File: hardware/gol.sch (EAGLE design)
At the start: 70 parts, among them J1 TC2050-IDC, J2 2057-MCR-B-S-RA-TSMT-NP-CS4-T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, U1 STM32F072CBT, U2 AP2111H-3.3TRG1SOT-223_DIO-M

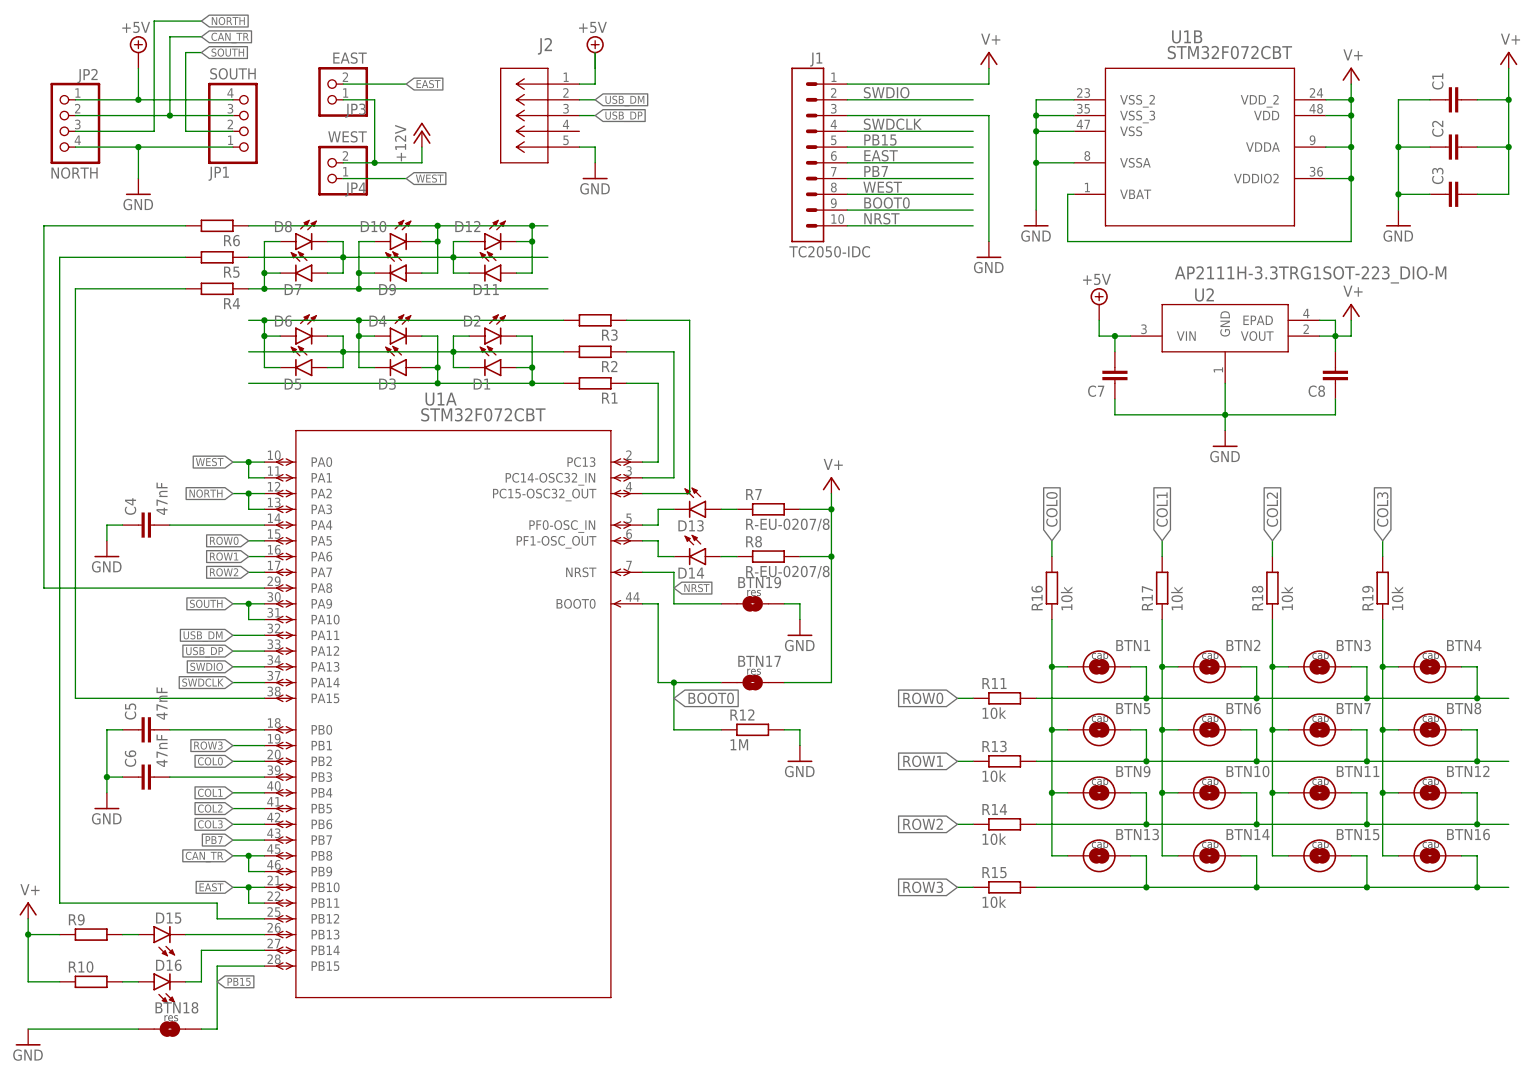
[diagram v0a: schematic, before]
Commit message: Finishes rerouting the row/col ports
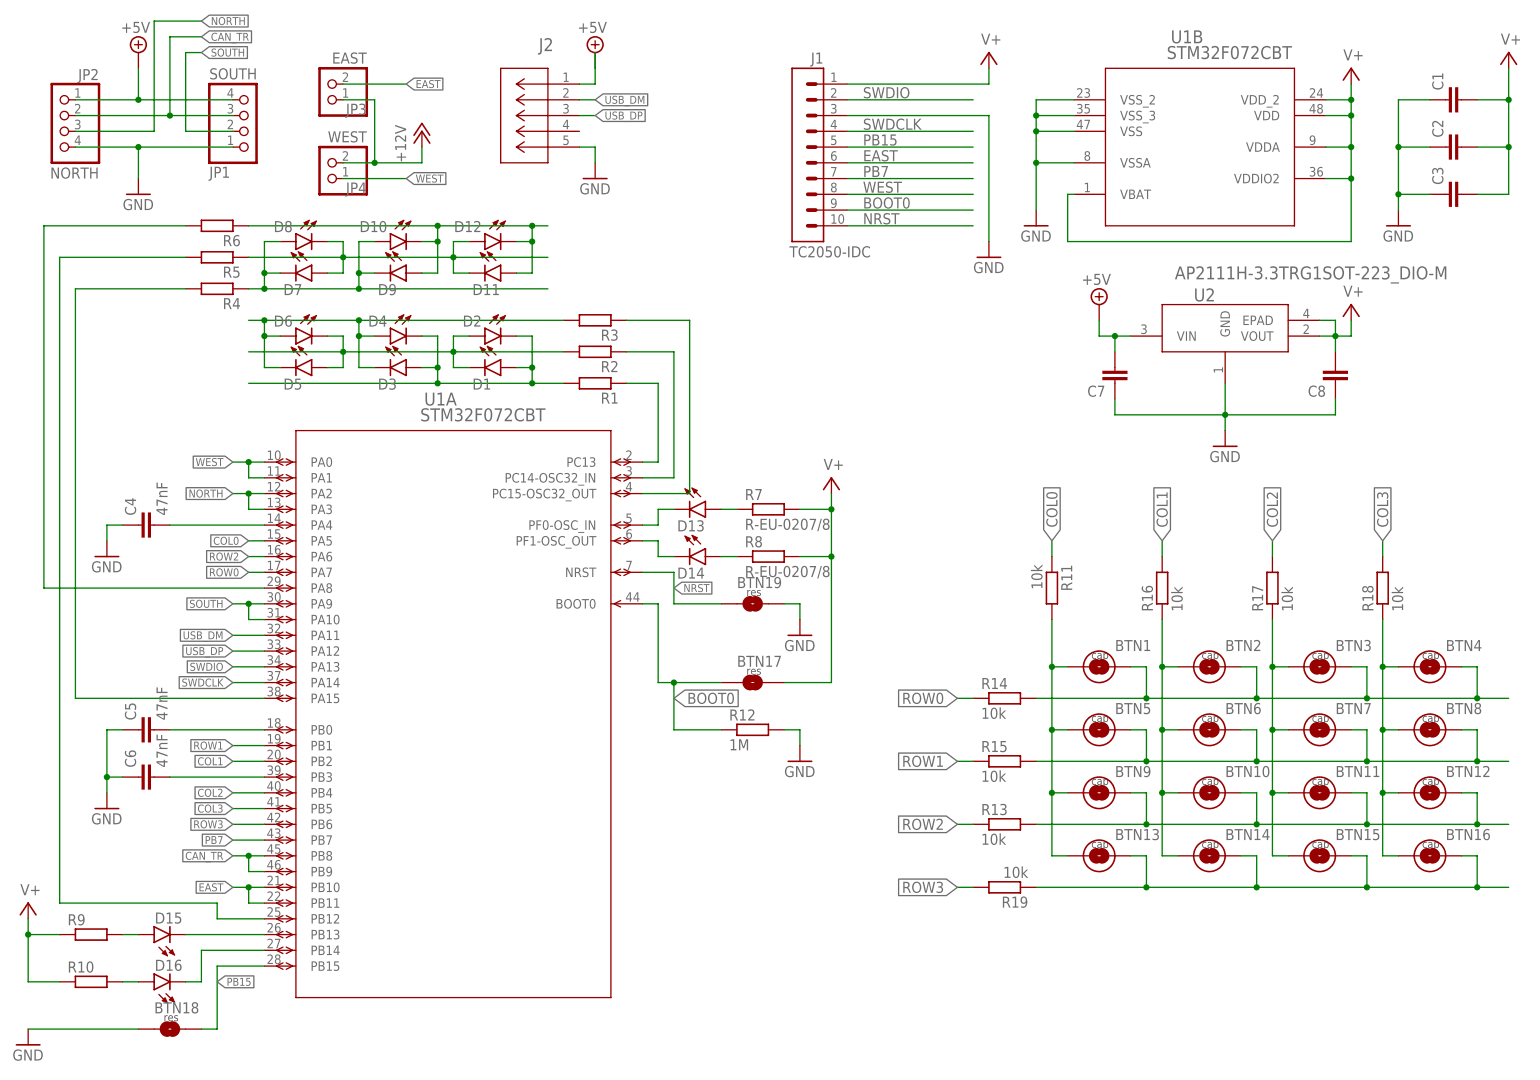
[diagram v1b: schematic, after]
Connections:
- net COL0: now also R11.1, U1A.PA5; no longer R16.2, U1A.PB2
- net COL1: now also R16.2, U1A.PB2; no longer R17.2, U1A.PB4
- net COL2: now also R17.2, U1A.PB4; no longer R18.2, U1A.PB5
- net COL3: now also R18.2, U1A.PB5; no longer R19.2, U1A.PB6
- net IN_COL0: now also R11.2; no longer R16.1
- net IN_COL1: now also R16.1; no longer R17.1
- net IN_COL2: now also R17.1; no longer R18.1
- net IN_COL3: now also R18.1; no longer R19.1
- net IN_ROW0: now also R14.2; no longer R11.2
- net IN_ROW1: now also R15.2; no longer R13.2
- net IN_ROW2: now also R13.2; no longer R14.2
- net IN_ROW3: now also R19.1; no longer R15.2
- net ROW0: now also R14.1, U1A.PA7; no longer R11.1, U1A.PA5
- net ROW1: now also R15.1, U1A.PB1; no longer R13.1, U1A.PA6
- net ROW2: now also R13.1, U1A.PA6; no longer R14.1, U1A.PA7
- net ROW3: now also R19.2, U1A.PB6; no longer R15.1, U1A.PB1
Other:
- moved on the sheet: R11, R13, R14, R15, R16, R17, R18, R19

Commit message: more routing.
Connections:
- net OUTA-L2: now also R3.1; no longer R2.1
- net OUTA-L3: now also R2.1; no longer R3.1
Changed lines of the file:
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@@
 <net name="OUTA-L2" class="0">
 <segment>
-<pinref part="R2" gate="G$1" pin="1"/>
 <pinref part="U1" gate="A" pin="PC14-OSC32_IN"/>
-<wire x1="104.14" y1="119.38" x2="111.76" y2="119.38" width="0.1524" layer="91"/>
-<wire x1="111.76" y1="119.38" x2="111.76" y2="99.06" width="0.1524" layer="91"/>
+<wire x1="111.76" y1="124.46" x2="111.76" y2="99.06" width="0.1524" layer="91"/>
 <wire x1="111.76" y1="99.06" x2="106.68" y2="99.06" width="0.1524" layer="91"/>
+<pinref part="R3" gate="G$1" pin="1"/>
+<wire x1="111.76" y1="124.46" x2="104.14" y2="124.46" width="0.1524" layer="91"/>
 </segment>
 </net>
@@
 <pinref part="U1" gate="A" pin="PC15-OSC32_OUT"/>
 <wire x1="106.68" y1="96.52" x2="114.3" y2="96.52" width="0.1524" layer="91"/>
-<wire x1="114.3" y1="96.52" x2="114.3" y2="124.46" width="0.1524" layer="91"/>
-<wire x1="114.3" y1="124.46" x2="104.14" y2="124.46" width="0.1524" layer="91"/>
-<pinref part="R3" gate="G$1" pin="1"/>
+<wire x1="114.3" y1="96.52" x2="114.3" y2="119.38" width="0.1524" layer="91"/>
+<pinref part="R2" gate="G$1" pin="1"/>
+<wire x1="114.3" y1="119.38" x2="104.14" y2="119.38" width="0.1524" layer="91"/>
 </segment>
 </net>

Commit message: More routing.
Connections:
- net OUTA-L1: now also R3.1; no longer R1.1
- net OUTA-L2: now also R1.1; no longer R3.1
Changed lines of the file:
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@@
 <segment>
 <pinref part="U1" gate="A" pin="PC14-OSC32_IN"/>
-<wire x1="111.76" y1="124.46" x2="111.76" y2="99.06" width="0.1524" layer="91"/>
+<wire x1="111.76" y1="114.3" x2="111.76" y2="99.06" width="0.1524" layer="91"/>
 <wire x1="111.76" y1="99.06" x2="106.68" y2="99.06" width="0.1524" layer="91"/>
-<pinref part="R3" gate="G$1" pin="1"/>
-<wire x1="111.76" y1="124.46" x2="104.14" y2="124.46" width="0.1524" layer="91"/>
+<pinref part="R1" gate="G$1" pin="1"/>
+<wire x1="111.76" y1="114.3" x2="104.14" y2="114.3" width="0.1524" layer="91"/>
 </segment>
 </net>
@@
 <pinref part="U1" gate="A" pin="PC13"/>
 <wire x1="106.68" y1="101.6" x2="109.22" y2="101.6" width="0.1524" layer="91"/>
-<wire x1="109.22" y1="101.6" x2="109.22" y2="114.3" width="0.1524" layer="91"/>
-<pinref part="R1" gate="G$1" pin="1"/>
-<wire x1="109.22" y1="114.3" x2="104.14" y2="114.3" width="0.1524" layer="91"/>
+<wire x1="109.22" y1="101.6" x2="109.22" y2="124.46" width="0.1524" layer="91"/>
+<pinref part="R3" gate="G$1" pin="1"/>
+<wire x1="109.22" y1="124.46" x2="104.14" y2="124.46" width="0.1524" layer="91"/>
 </segment>
 </net>

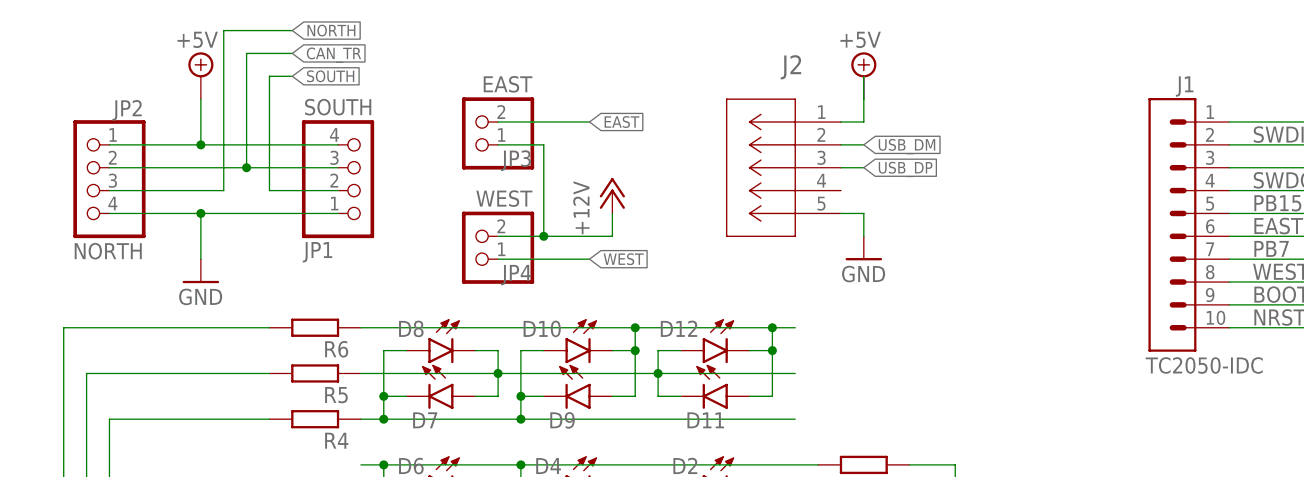
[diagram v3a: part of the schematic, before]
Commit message: Adds 4-pin connector to east and west as well. Routes all remaining airwires.
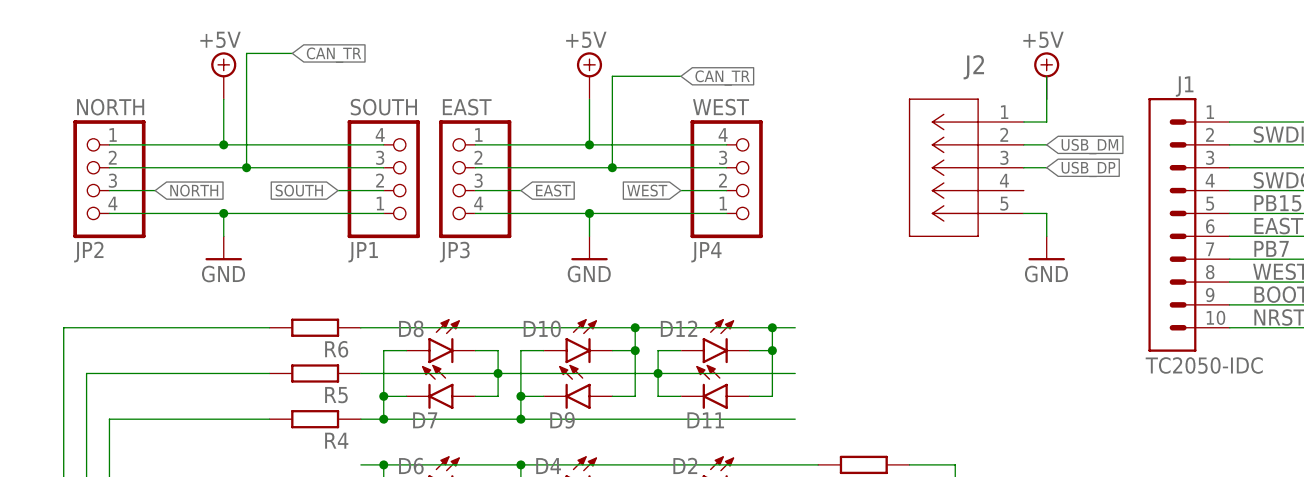
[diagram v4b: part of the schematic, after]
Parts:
- JP3, JP4: device parts:PINHD-1X2 -> parts:PINHD-1X04
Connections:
- removed net +12V: JP3.1, JP4.2
- net +5V: now also JP3.1, JP4.4
- net CAN_TR: now also JP3.2, JP4.3
- net EAST: now also JP3.3; no longer JP3.2
- net GND: now also JP3.4, JP4.1
- net WEST: now also JP4.2; no longer JP4.1
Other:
- moved on the sheet: J2, JP1

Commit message: Places parts labels on top and bottom layer.
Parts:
- renumbered JP1 to SOUTH, JP2 to NORTH, JP3 to EAST, JP4 to WEST
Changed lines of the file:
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@@
 <part name="R9" library="parts" deviceset="R-EU-0207/8" device=""/>
 <part name="R10" library="parts" deviceset="R-EU-0207/8" device=""/>
-<part name="JP1" library="pinhead" library_urn="urn:adsk.eagle:library:325" deviceset="PINHD-1X4" device="/90" package3d_urn="urn:adsk.eagle:package:22404/2" value="SOUTH"/>
-<part name="JP2" library="pinhead" library_urn="urn:adsk.eagle:library:325" deviceset="PINHD-1X4" device="/90" package3d_urn="urn:adsk.eagle:package:22404/2" value="NORTH"/>
+<part name="SOUTH" library="pinhead" library_urn="urn:adsk.eagle:library:325" deviceset="PINHD-1X4" device="/90" package3d_urn="urn:adsk.eagle:package:22404/2" value="SOUTH"/>
+<part name="NORTH" library="pinhead" library_urn="urn:adsk.eagle:library:325" deviceset="PINHD-1X4" device="/90" package3d_urn="urn:adsk.eagle:package:22404/2" value="NORTH"/>
 <part name="GND3" library="supply1" library_urn="urn:adsk.eagle:library:371" deviceset="GND" device=""/>
-<part name="JP3" library="parts" deviceset="PINHD-1X04" device="" value="EAST"/>
-<part name="JP4" library="parts" deviceset="PINHD-1X04" device="" value="WEST"/>
+<part name="EAST" library="parts" deviceset="PINHD-1X04" device="" value="EAST"/>
+<part name="WEST" library="parts" deviceset="PINHD-1X04" device="" value="WEST"/>
 <part name="C4" library="rcl" library_urn="urn:adsk.eagle:library:334" deviceset="C-EU" device="C0603" package3d_urn="urn:adsk.eagle:package:23616/2" value="47nF"/>
 <part name="C5" library="rcl" library_urn="urn:adsk.eagle:library:334" deviceset="C-EU" device="C0603" package3d_urn="urn:adsk.eagle:package:23616/2" value="47nF"/>
@@
 <attribute name="NAME" x="13.97" y="19.2786" size="1.778" layer="95"/>
 </instance>
-<instance part="JP1" gate="A" x="48.26" y="157.48" smashed="yes" rot="MR180">
+<instance part="SOUTH" gate="A" x="48.26" y="157.48" smashed="yes" rot="MR180">
 <attribute name="NAME" x="41.91" y="149.225" size="1.778" layer="95" rot="MR180"/>
-<attribute name="VALUE" x="41.91" y="165.1" size="1.778" layer="96" rot="MR180"/>
-</instance>
-<instance part="JP2" gate="A" x="12.7" y="154.94" smashed="yes" rot="MR0">
+</instance>
+<instance part="NORTH" gate="A" x="12.7" y="154.94" smashed="yes" rot="MR0">
 <attribute name="NAME" x="11.43" y="149.225" size="1.778" layer="95" rot="MR180"/>
-<attribute name="VALUE" x="11.43" y="165.1" size="1.778" layer="96" rot="MR180"/>
 </instance>
 <instance part="GND3" gate="1" x="27.94" y="147.32" smashed="yes">
 <attribute name="VALUE" x="25.4" y="144.78" size="1.778" layer="96"/>
 </instance>
-<instance part="JP3" gate="G$1" x="53.34" y="154.94" smashed="yes" rot="MR0">
+<instance part="EAST" gate="G$1" x="53.34" y="154.94" smashed="yes" rot="MR0">
 <attribute name="NAME" x="52.07" y="149.225" size="1.778" layer="95" rot="MR180"/>
-<attribute name="VALUE" x="52.07" y="165.1" size="1.778" layer="96" rot="MR180"/>
-</instance>
-<instance part="JP4" gate="G$1" x="86.36" y="157.48" smashed="yes" rot="MR180">
+</instance>
+<instance part="WEST" gate="G$1" x="86.36" y="157.48" smashed="yes" rot="MR180">
 <attribute name="NAME" x="80.01" y="149.225" size="1.778" layer="95" rot="MR180"/>
-<attribute name="VALUE" x="80.01" y="165.1" size="1.778" layer="96" rot="MR180"/>
 </instance>
 <instance part="C4" gate="G$1" x="25.4" y="91.44" smashed="yes" rot="R90">
@@
 </segment>
 <segment>
-<pinref part="JP2" gate="A" pin="4"/>
-<pinref part="JP1" gate="A" pin="1"/>
+<pinref part="NORTH" gate="A" pin="4"/>
+<pinref part="SOUTH" gate="A" pin="1"/>
 <wire x1="15.24" y1="152.4" x2="27.94" y2="152.4" width="0.1524" layer="91"/>
 <pinref part="GND3" gate="1" pin="GND"/>
@@
 </segment>
 <segment>
-<pinref part="JP3" gate="G$1" pin="4"/>
-<pinref part="JP4" gate="G$1" pin="1"/>
+<pinref part="EAST" gate="G$1" pin="4"/>
+<pinref part="WEST" gate="G$1" pin="1"/>
 <wire x1="55.88" y1="152.4" x2="68.58" y2="152.4" width="0.1524" layer="91"/>
 <pinref part="GND12" gate="1" pin="GND"/>
@@
 <net name="CAN_TR" class="0">
 <segment>
-<pinref part="JP2" gate="A" pin="2"/>
-<pinref part="JP1" gate="A" pin="3"/>
+<pinref part="NORTH" gate="A" pin="2"/>
+<pinref part="SOUTH" gate="A" pin="3"/>
 <wire x1="15.24" y1="157.48" x2="30.48" y2="157.48" width="0.1524" layer="91"/>
 <wire x1="30.48" y1="157.48" x2="45.72" y2="157.48" width="0.1524" layer="91"/>
@@
 <wire x1="71.12" y1="167.64" x2="78.74" y2="167.64" width="0.1524" layer="91"/>
 <wire x1="71.12" y1="167.64" x2="71.12" y2="157.48" width="0.1524" layer="91"/>
-<pinref part="JP4" gate="G$1" pin="3"/>
+<pinref part="WEST" gate="G$1" pin="3"/>
 <wire x1="71.12" y1="157.48" x2="83.82" y2="157.48" width="0.1524" layer="91"/>
-<pinref part="JP3" gate="G$1" pin="2"/>
+<pinref part="EAST" gate="G$1" pin="2"/>
 <wire x1="71.12" y1="157.48" x2="55.88" y2="157.48" width="0.1524" layer="91"/>
 <junction x="71.12" y="157.48"/>
@@
 <net name="NORTH" class="0">
 <segment>
-<pinref part="JP2" gate="A" pin="3"/>
+<pinref part="NORTH" gate="A" pin="3"/>
 <wire x1="15.24" y1="154.94" x2="20.32" y2="154.94" width="0.1524" layer="91"/>
 <label x="20.32" y="154.94" size="1.27" layer="95" xref="yes"/>
@@
 <net name="SOUTH" class="0">
 <segment>
-<pinref part="JP1" gate="A" pin="2"/>
+<pinref part="SOUTH" gate="A" pin="2"/>
 <wire x1="45.72" y1="154.94" x2="40.64" y2="154.94" width="0.1524" layer="91"/>
 <label x="40.64" y="154.94" size="1.27" layer="95" rot="R180" xref="yes"/>
@@
 <segment>
 <label x="60.96" y="154.94" size="1.27" layer="95" xref="yes"/>
-<pinref part="JP3" gate="G$1" pin="3"/>
+<pinref part="EAST" gate="G$1" pin="3"/>
 <wire x1="60.96" y1="154.94" x2="55.88" y2="154.94" width="0.1524" layer="91"/>
 </segment>
@@
 <segment>
 <label x="78.74" y="154.94" size="1.27" layer="95" rot="R180" xref="yes"/>
-<pinref part="JP4" gate="G$1" pin="2"/>
+<pinref part="WEST" gate="G$1" pin="2"/>
 <wire x1="78.74" y1="154.94" x2="83.82" y2="154.94" width="0.1524" layer="91"/>
 </segment>
@@
 </segment>
 <segment>
-<pinref part="JP2" gate="A" pin="1"/>
-<pinref part="JP1" gate="A" pin="4"/>
+<pinref part="NORTH" gate="A" pin="1"/>
+<pinref part="SOUTH" gate="A" pin="4"/>
 <wire x1="15.24" y1="160.02" x2="27.94" y2="160.02" width="0.1524" layer="91"/>
 <pinref part="SUPPLY7" gate="+5V" pin="+5V"/>
@@
 </segment>
 <segment>
-<pinref part="JP3" gate="G$1" pin="1"/>
+<pinref part="EAST" gate="G$1" pin="1"/>
 <wire x1="55.88" y1="160.02" x2="68.58" y2="160.02" width="0.1524" layer="91"/>
 <pinref part="SUPPLY10" gate="+5V" pin="+5V"/>
 <wire x1="68.58" y1="160.02" x2="68.58" y2="165.1" width="0.1524" layer="91"/>
-<pinref part="JP4" gate="G$1" pin="4"/>
+<pinref part="WEST" gate="G$1" pin="4"/>
 <wire x1="68.58" y1="160.02" x2="83.82" y2="160.02" width="0.1524" layer="91"/>
 <junction x="68.58" y="160.02"/>

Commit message: more labeling work. Updates parts so that they have outlines.
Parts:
- R12: value 1M -> 470k
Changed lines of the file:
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@@
 <part name="D16" library="parts" deviceset="LED-5MM" device=""/>
 <part name="SUPPLY4" library="supply2" library_urn="urn:adsk.eagle:library:372" deviceset="V+" device=""/>
-<part name="R12" library="rcl" library_urn="urn:adsk.eagle:library:334" deviceset="R-EU_" device="R0603" package3d_urn="urn:adsk.eagle:package:23555/3" value="1M"/>
+<part name="R12" library="rcl" library_urn="urn:adsk.eagle:library:334" deviceset="R-EU_" device="R0603" package3d_urn="urn:adsk.eagle:package:23555/3" value="470k"/>
 <part name="GND6" library="supply1" library_urn="urn:adsk.eagle:library:371" deviceset="GND" device=""/>
 <part name="BTN17" library="parts" deviceset="BUTTON-RES" device="" value="BOOT"/>
@@
 <instance part="R7" gate="G$1" x="127" y="93.98" smashed="yes">
 <attribute name="NAME" x="123.19" y="95.4786" size="1.778" layer="95"/>
-<attribute name="VALUE" x="123.19" y="90.678" size="1.778" layer="96"/>
 </instance>
 <instance part="R8" gate="G$1" x="127" y="86.36" smashed="yes">
 <attribute name="NAME" x="123.19" y="87.8586" size="1.778" layer="95"/>
-<attribute name="VALUE" x="123.19" y="83.058" size="1.778" layer="96"/>
 </instance>
 <instance part="R9" gate="G$1" x="17.78" y="25.4" smashed="yes">
